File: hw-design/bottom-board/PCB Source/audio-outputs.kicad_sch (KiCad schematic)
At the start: 73 parts, among them J10 NYS215, J9 NYS215, K1 G6S-2, K2 G6S-2, Q1 2N7002, Q2 2N7002, U11 RC4580ID, U12 RC4580ID

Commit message: fix prev commit
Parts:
- gave numbers to parts that had none: 4
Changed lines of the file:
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@@
   (symbol (lib_id "bottom-board-rescue:R_Small-Device") (at 152.019 17.526 270) (unit 1)
     (in_bom yes) (on_board yes)
-    (property "Reference" "R?" (id 0) (at 150.114 13.716 90)
+    (property "Reference" "R147" (id 0) (at 150.114 13.716 90)
       (effects (font (size 1.27 1.27)) (justify left))
     )
@@
   (symbol (lib_id "bottom-board-rescue:R_Small-Device") (at 152.146 23.368 270) (unit 1)
     (in_bom yes) (on_board yes)
-    (property "Reference" "R?" (id 0) (at 150.241 19.558 90)
+    (property "Reference" "R148" (id 0) (at 150.241 19.558 90)
       (effects (font (size 1.27 1.27)) (justify left))
     )
@@
   (symbol (lib_id "bottom-board-rescue:R_Small-Device") (at 154.178 82.042 270) (unit 1)
     (in_bom yes) (on_board yes)
-    (property "Reference" "R?" (id 0) (at 152.273 78.232 90)
+    (property "Reference" "R149" (id 0) (at 152.273 78.232 90)
       (effects (font (size 1.27 1.27)) (justify left))
     )
@@
   (symbol (lib_id "bottom-board-rescue:R_Small-Device") (at 154.305 87.884 270) (unit 1)
     (in_bom yes) (on_board yes)
-    (property "Reference" "R?" (id 0) (at 152.4 84.074 90)
+    (property "Reference" "R150" (id 0) (at 152.4 84.074 90)
       (effects (font (size 1.27 1.27)) (justify left))
     )

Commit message: update fabrication data
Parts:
- C51, C52: MPN2 (none) -> GCM188R71C104KA37D
- C53, C54: MPN2 (none) -> CL21A226MPQNNNE
- D7: MPN NO DONT PLACE -> DO NOT PLACE; MPN2 (none) -> 1N4148WX-TP
- D8: MPN2 (none) -> 1N4148WX-TP
- Q1, Q2: MPN2 (none) -> 2N7002P 215
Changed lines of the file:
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@@
   (title_block
     (title "MOD DuoX - Bottom Board")
-    (date "2021-11-11")
-    (rev "Rev 1.05")
+    (date "2022-01-26")
+    (rev "Rev 2.0P2")
     (company "MOD Devices GmbH")
     (comment 1 "DuoX Audio processing board")
     (comment 2 "https://github.com/moddevices/mod-hw-duoX")
-    (comment 3 "Inp Power: 12V 700mA")
-    (comment 4 "USB outp Power: 500mA")
+    (comment 3 "Inp Power: 12V 1A")
   )
   (junction (at 166.243 38.989) (diameter 0) (color 0 0 0 0)
@@
       (effects (font (size 1.524 1.524)) hide)
     )
+    (property "MPN2" "2N7002P 215" (id 5) (at 164.592 68.453 0)
+      (effects (font (size 1.524 1.524)) hide)
+    )
     (pin "1")
     (pin "2")
@@
       (effects (font (size 1.27 1.27)) hide)
     )
-    (property "MPN" "NO DONT PLACE" (id 4) (at -34.671 135.509 0)
-      (effects (font (size 1.27 1.27)) hide)
+    (property "MPN" "DO NOT PLACE" (id 4) (at -34.671 135.509 0)
+      (effects (font (size 1.27 1.27)) hide)
+    )
+    (property "MPN2" "1N4148WX-TP" (id 5) (at 152.019 61.849 0)
+      (effects (font (size 1.524 1.524)) hide)
     )
     (pin "1")
@@
       (effects (font (size 1.27 1.27)) hide)
     )
+    (property "MPN2" "GCM188R71C104KA37D" (id 5) (at 132.969 66.929 90)
+      (effects (font (size 1.524 1.524)) hide)
+    )
     (pin "1")
     (pin "2")
@@
     (property "MPN" "DO NOT PLACE" (id 4) (at 270.383 -4.953 0)
       (effects (font (size 1.27 1.27)) hide)
+    )
+    (property "MPN2" "GCM188R71C104KA37D" (id 5) (at 135.763 130.937 90)
+      (effects (font (size 1.524 1.524)) hide)
     )
     (pin "1")
@@
       (effects (font (size 1.27 1.27)) hide)
     )
+    (property "MPN2" "1N4148WX-TP" (id 5) (at 154.813 125.857 0)
+      (effects (font (size 1.524 1.524)) hide)
+    )
     (pin "1")
     (pin "2")
@@
     )
     (property "MPN" "DO NOT PLACE" (id 4) (at 167.386 133.858 0)
+      (effects (font (size 1.524 1.524)) hide)
+    )
+    (property "MPN2" "2N7002P 215" (id 5) (at 167.386 133.858 0)
       (effects (font (size 1.524 1.524)) hide)
     )
@@
       (effects (font (size 1.27 1.27)) hide)
     )
+    (property "MPN2" "CL21A226MPQNNNE" (id 5) (at 138.049 66.929 90)
+      (effects (font (size 1.524 1.524)) hide)
+    )
     (pin "1")
     (pin "2")
@@
       (effects (font (size 1.27 1.27)) hide)
     )
-    (pin "1")
+    (property "MPN2" "CL21A226MPQNNNE" (id 5) (at 140.843 130.937 90)
+      (effects (font (size 1.524 1.524)) hide)
+    )
+    (pin "1")

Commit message: update fabrication data
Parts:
- U11, U12: value RC4580ID -> LM833DR2G; MPN OPA1678IDR -> LM833DR2G
- U11, U12: value RC4580ID -> LM833DR2G; MPN RC4580ID -> LM833DR2G
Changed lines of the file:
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@@
     (in_bom yes) (on_board yes)
     (property "Reference" "U11" (id 0) (at 77.089 23.749 0))
-    (property "Value" "RC4580ID" (id 1) (at 77.089 25.654 0))
+    (property "Value" "LM833DR2G" (id 1) (at 77.089 25.654 0))
     (property "Footprint" "Package_SO:SOIC-8_3.9x4.9mm_P1.27mm" (id 2) (at 77.089 31.369 0)
       (effects (font (size 1.27 1.27)) hide)
@@
       (effects (font (size 1.27 1.27)) hide)
     )
-    (property "MPN" "OPA1678IDR" (id 4) (at -5.461 73.279 0)
+    (property "MPN" "LM833DR2G" (id 4) (at -5.461 73.279 0)
       (effects (font (size 1.27 1.27)) hide)
     )
@@
     (in_bom yes) (on_board yes)
     (property "Reference" "U11" (id 0) (at 45.085 168.91 90))
-    (property "Value" "RC4580ID" (id 1) (at 46.99 168.91 90))
+    (property "Value" "LM833DR2G" (id 1) (at 46.99 168.91 90))
     (property "Footprint" "Package_SO:SOIC-8_3.9x4.9mm_P1.27mm" (id 2) (at 45.085 168.91 0)
       (effects (font (size 1.27 1.27)) hide)
@@
       (effects (font (size 1.27 1.27)) hide)
     )
-    (property "MPN" "OPA1678IDR" (id 4) (at 19.685 337.82 0)
+    (property "MPN" "LM833DR2G" (id 4) (at 19.685 337.82 0)
       (effects (font (size 1.27 1.27)) hide)
     )
@@
     (in_bom yes) (on_board yes)
     (property "Reference" "U11" (id 0) (at 77.216 73.025 0))
-    (property "Value" "RC4580ID" (id 1) (at 77.216 71.12 0))
+    (property "Value" "LM833DR2G" (id 1) (at 77.216 71.12 0))
     (property "Footprint" "Package_SO:SOIC-8_3.9x4.9mm_P1.27mm" (id 2) (at 77.216 65.405 0)
       (effects (font (size 1.27 1.27)) hide)
@@
       (effects (font (size 1.27 1.27)) hide)
     )
-    (property "MPN" "RC4580ID" (id 4) (at -5.334 23.495 0)
+    (property "MPN" "LM833DR2G" (id 4) (at -5.334 23.495 0)
       (effects (font (size 1.27 1.27)) hide)
     )
@@
     (in_bom yes) (on_board yes)
     (property "Reference" "U12" (id 0) (at 55.245 169.545 90))
-    (property "Value" "RC4580ID" (id 1) (at 57.15 168.91 90))
+    (property "Value" "LM833DR2G" (id 1) (at 57.15 168.91 90))
     (property "Footprint" "Package_SO:SOIC-8_3.9x4.9mm_P1.27mm" (id 2) (at 55.245 168.91 0)
       (effects (font (size 1.27 1.27)) hide)
@@
       (effects (font (size 1.27 1.27)) hide)
     )
-    (property "MPN" "OPA1678IDR" (id 4) (at 29.845 337.82 0)
+    (property "MPN" "LM833DR2G" (id 4) (at 29.845 337.82 0)
       (effects (font (size 1.27 1.27)) hide)
     )
@@
     (in_bom yes) (on_board yes)
     (property "Reference" "U12" (id 0) (at 77.47 87.757 0))
-    (property "Value" "RC4580ID" (id 1) (at 77.47 89.662 0))
+    (property "Value" "LM833DR2G" (id 1) (at 77.47 89.662 0))
     (property "Footprint" "Package_SO:SOIC-8_3.9x4.9mm_P1.27mm" (id 2) (at 77.47 95.377 0)
       (effects (font (size 1.27 1.27)) hide)
@@
       (effects (font (size 1.27 1.27)) hide)
     )
-    (property "MPN" "OPA1678IDR" (id 4) (at -5.08 137.287 0)
+    (property "MPN" "LM833DR2G" (id 4) (at -5.08 137.287 0)
       (effects (font (size 1.27 1.27)) hide)
     )
@@
     (in_bom yes) (on_board yes)
     (property "Reference" "U12" (id 0) (at 80.264 137.795 0))
-    (property "Value" "RC4580ID" (id 1) (at 80.264 135.89 0))
+    (property "Value" "LM833DR2G" (id 1) (at 80.264 135.89 0))
     (property "Footprint" "Package_SO:SOIC-8_3.9x4.9mm_P1.27mm" (id 2) (at 80.264 130.175 0)
       (effects (font (size 1.27 1.27)) hide)
@@
       (effects (font (size 1.27 1.27)) hide)
     )
-    (property "MPN" "RC4580ID" (id 4) (at -2.286 88.265 0)
+    (property "MPN" "LM833DR2G" (id 4) (at -2.286 88.265 0)
       (effects (font (size 1.27 1.27)) hide)
     )

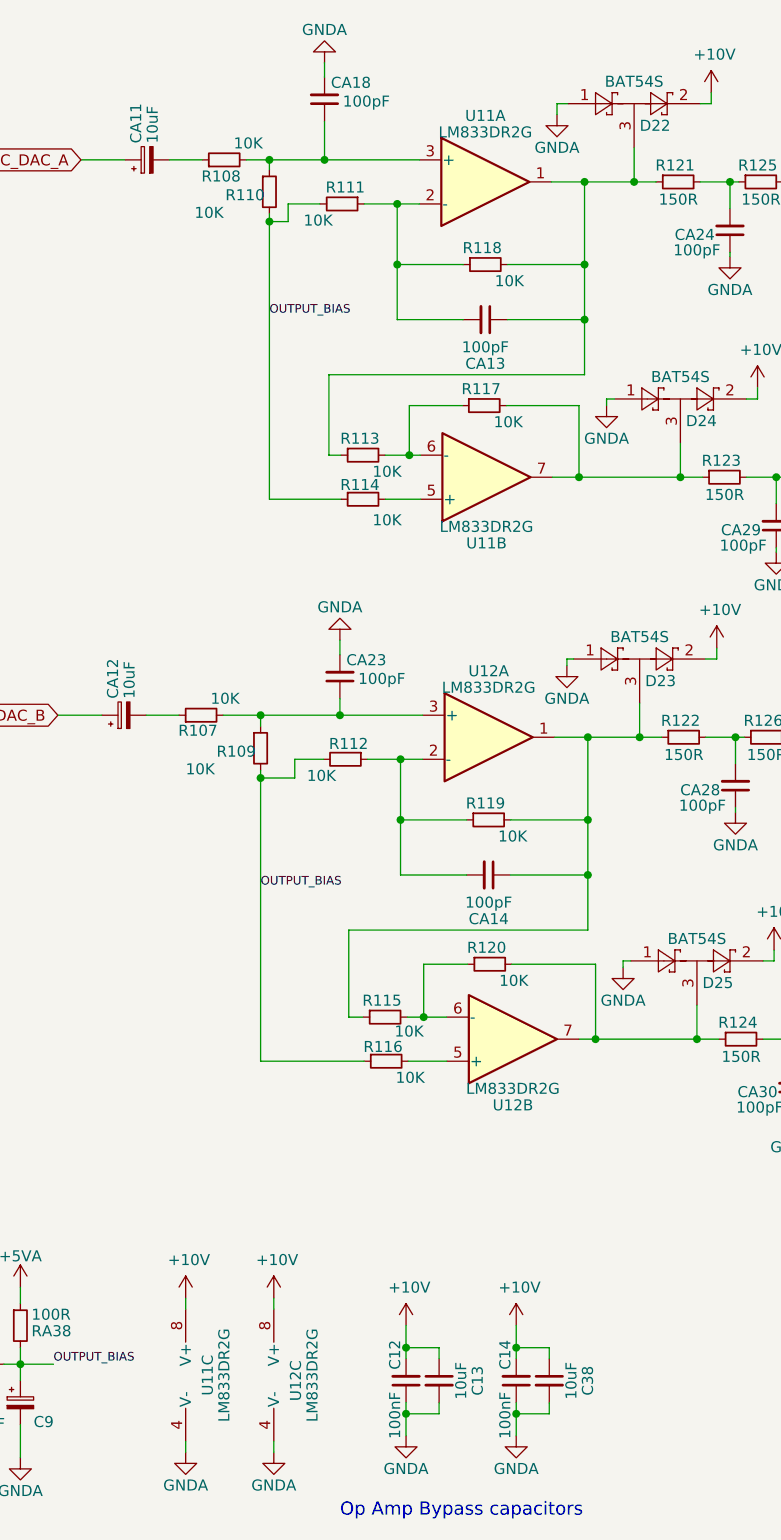
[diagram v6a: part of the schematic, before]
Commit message: mainboard: correct CC TX pin + update fabrication files
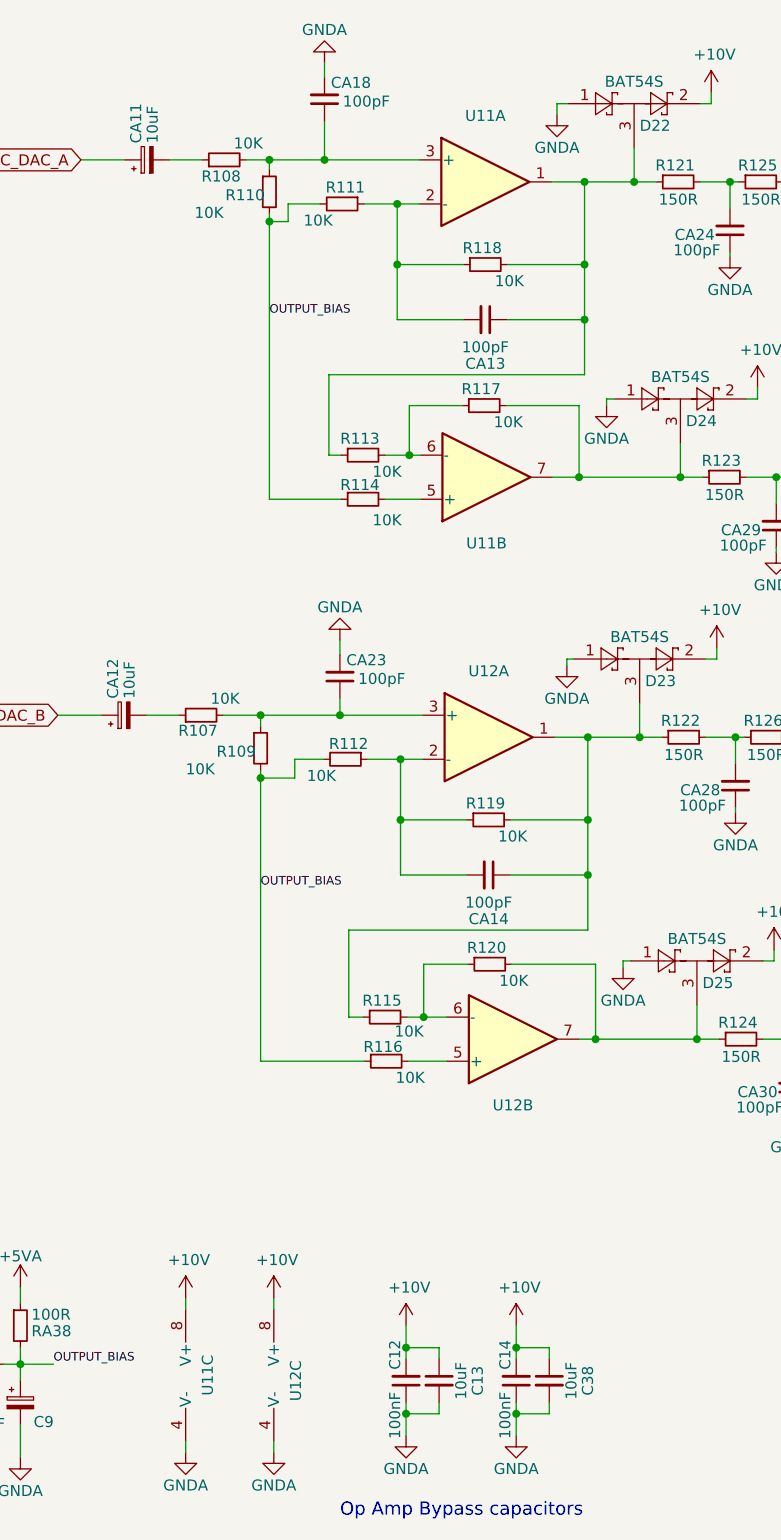
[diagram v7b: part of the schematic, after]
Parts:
- U11, U12: value LM833DR2G -> (none); footprint Package_SO:SOIC-8_3.9x4.9mm_P1.27mm -> (none); MPN LM833DR2G -> OPA1678IDR; MPN2 (none) -> LM833DR2G
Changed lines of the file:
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@@
     (in_bom yes) (on_board yes)
     (property "Reference" "U11" (id 0) (at 77.089 23.749 0))
-    (property "Value" "LM833DR2G" (id 1) (at 77.089 25.654 0))
-    (property "Footprint" "Package_SO:SOIC-8_3.9x4.9mm_P1.27mm" (id 2) (at 77.089 31.369 0)
+    (property "Value" "" (id 1) (at 77.089 25.654 0))
+    (property "Footprint" "" (id 2) (at 77.089 31.369 0)
       (effects (font (size 1.27 1.27)) hide)
     )
@@
       (effects (font (size 1.27 1.27)) hide)
     )
-    (property "MPN" "LM833DR2G" (id 4) (at -5.461 73.279 0)
+    (property "MPN" "OPA1678IDR" (id 4) (at -5.461 73.279 0)
       (effects (font (size 1.27 1.27)) hide)
+    )
+    (property "MPN2" "LM833DR2G" (id 5) (at 77.216 65.405 0)
+      (effects (font (size 1.524 1.524)) hide)
     )
     (pin "1")
     (pin "2")
     (pin "3")
+    (pin "5")
+    (pin "6")
+    (pin "7")
+    (pin "4")
+    (pin "8")
   )
   (symbol (lib_id "bottom-board-rescue:LM4562-Amplifier_Operational") (at 45.085 168.91 0) (unit 3)
     (in_bom yes) (on_board yes)
     (property "Reference" "U11" (id 0) (at 45.085 168.91 90))
-    (property "Value" "LM833DR2G" (id 1) (at 46.99 168.91 90))
-    (property "Footprint" "Package_SO:SOIC-8_3.9x4.9mm_P1.27mm" (id 2) (at 45.085 168.91 0)
+    (property "Value" "" (id 1) (at 46.99 168.91 90))
+    (property "Footprint" "" (id 2) (at 45.085 168.91 0)
       (effects (font (size 1.27 1.27)) hide)
     )
@@
       (effects (font (size 1.27 1.27)) hide)
     )
-    (property "MPN" "LM833DR2G" (id 4) (at 19.685 337.82 0)
+    (property "MPN" "OPA1678IDR" (id 4) (at 19.685 337.82 0)
       (effects (font (size 1.27 1.27)) hide)
     )
+    (property "MPN2" "LM833DR2G" (id 5) (at 77.216 65.405 0)
+      (effects (font (size 1.524 1.524)) hide)
+    )
+    (pin "1")
+    (pin "2")
+    (pin "3")
+    (pin "5")
+    (pin "6")
+    (pin "7")
     (pin "4")
     (pin "8")
@@
     (in_bom yes) (on_board yes)
     (property "Reference" "U11" (id 0) (at 77.216 73.025 0))
-    (property "Value" "LM833DR2G" (id 1) (at 77.216 71.12 0))
-    (property "Footprint" "Package_SO:SOIC-8_3.9x4.9mm_P1.27mm" (id 2) (at 77.216 65.405 0)
+    (property "Value" "" (id 1) (at 77.216 71.12 0))
+    (property "Footprint" "" (id 2) (at 77.216 65.405 0)
       (effects (font (size 1.27 1.27)) hide)
     )
@@
       (effects (font (size 1.27 1.27)) hide)
     )
-    (property "MPN" "LM833DR2G" (id 4) (at -5.334 23.495 0)
+    (property "MPN" "OPA1678IDR" (id 4) (at -5.334 23.495 0)
       (effects (font (size 1.27 1.27)) hide)
     )
+    (property "MPN2" "LM833DR2G" (id 5) (at 77.216 65.405 0)
+      (effects (font (size 1.524 1.524)) hide)
+    )
+    (pin "1")
+    (pin "2")
+    (pin "3")
     (pin "5")
     (pin "6")
     (pin "7")
+    (pin "4")
+    (pin "8")
   )
   (symbol (lib_id "bottom-board-rescue:LM4562-Amplifier_Operational") (at 55.245 168.91 0) (unit 3)
     (in_bom yes) (on_board yes)
     (property "Reference" "U12" (id 0) (at 55.245 169.545 90))
-    (property "Value" "LM833DR2G" (id 1) (at 57.15 168.91 90))
-    (property "Footprint" "Package_SO:SOIC-8_3.9x4.9mm_P1.27mm" (id 2) (at 55.245 168.91 0)
+    (property "Value" "" (id 1) (at 57.15 168.91 90))
+    (property "Footprint" "" (id 2) (at 55.245 168.91 0)
       (effects (font (size 1.27 1.27)) hide)
     )
@@
       (effects (font (size 1.27 1.27)) hide)
     )
-    (property "MPN" "LM833DR2G" (id 4) (at 29.845 337.82 0)
+    (property "MPN" "OPA1678IDR" (id 4) (at 29.845 337.82 0)
       (effects (font (size 1.27 1.27)) hide)
     )
+    (property "MPN2" "LM833DR2G" (id 5) (at 77.47 95.377 0)
+      (effects (font (size 1.524 1.524)) hide)
+    )
+    (pin "1")
+    (pin "2")
+    (pin "3")
+    (pin "5")
+    (pin "6")
+    (pin "7")
     (pin "4")
     (pin "8")
@@
     (in_bom yes) (on_board yes)
     (property "Reference" "U12" (id 0) (at 77.47 87.757 0))
-    (property "Value" "LM833DR2G" (id 1) (at 77.47 89.662 0))
-    (property "Footprint" "Package_SO:SOIC-8_3.9x4.9mm_P1.27mm" (id 2) (at 77.47 95.377 0)
+    (property "Value" "" (id 1) (at 77.47 89.662 0))
+    (property "Footprint" "" (id 2) (at 77.47 95.377 0)
       (effects (font (size 1.27 1.27)) hide)
     )
@@
       (effects (font (size 1.27 1.27)) hide)
     )
-    (property "MPN" "LM833DR2G" (id 4) (at -5.08 137.287 0)
+    (property "MPN" "OPA1678IDR" (id 4) (at -5.08 137.287 0)
       (effects (font (size 1.27 1.27)) hide)
+    )
+    (property "MPN2" "LM833DR2G" (id 5) (at 77.47 95.377 0)
+      (effects (font (size 1.524 1.524)) hide)
     )
     (pin "1")
     (pin "2")
     (pin "3")
+    (pin "5")
+    (pin "6")
+    (pin "7")
+    (pin "4")
+    (pin "8")
   )
   (symbol (lib_id "bottom-board-rescue:LM4562-Amplifier_Operational") (at 80.264 130.175 0) (mirror x) (unit 2)
     (in_bom yes) (on_board yes)
     (property "Reference" "U12" (id 0) (at 80.264 137.795 0))
-    (property "Value" "LM833DR2G" (id 1) (at 80.264 135.89 0))
-    (property "Footprint" "Package_SO:SOIC-8_3.9x4.9mm_P1.27mm" (id 2) (at 80.264 130.175 0)
+    (property "Value" "" (id 1) (at 80.264 135.89 0))
+    (property "Footprint" "" (id 2) (at 80.264 130.175 0)
       (effects (font (size 1.27 1.27)) hide)
     )
@@
       (effects (font (size 1.27 1.27)) hide)
     )
-    (property "MPN" "LM833DR2G" (id 4) (at -2.286 88.265 0)
+    (property "MPN" "OPA1678IDR" (id 4) (at -2.286 88.265 0)
       (effects (font (size 1.27 1.27)) hide)
     )
+    (property "MPN2" "LM833DR2G" (id 5) (at 77.47 95.377 0)
+      (effects (font (size 1.524 1.524)) hide)
+    )
+    (pin "1")
+    (pin "2")
+    (pin "3")
     (pin "5")
     (pin "6")
     (pin "7")
+    (pin "4")
+    (pin "8")
   )
   (symbol (lib_id "bottom-board-rescue:R_Small-Device") (at 46.99 28.829 90) (unit 1)
